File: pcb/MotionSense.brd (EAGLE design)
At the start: 59.4 x 59.2 mm, 14 parts

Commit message: [UPDATE] connection missing bug fixing
connection to the ground was not done.
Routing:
- net N$4: track 93.7 -> 106.0 mm
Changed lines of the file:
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@@
 <wire x1="70.7009" y1="65.4431" x2="61.9252" y2="65.4431" width="0.4064" layer="1"/>
 <wire x1="69.6976" y1="56.0451" x2="72.1741" y2="58.5216" width="0.4064" layer="1"/>
-<wire x1="69.394" y1="22.8748" x2="69.3432" y2="31.8156" width="0" layer="19" extent="1-1"/>
+<wire x1="69.394" y1="22.8748" x2="72.958959375" y2="26.439759375" width="0.4064" layer="16"/>
+<wire x1="72.958959375" y1="26.439759375" x2="72.958959375" y2="28.971240625" width="0.4064" layer="16"/>
+<wire x1="72.958959375" y1="28.971240625" x2="70.1146" y2="31.8156" width="0.4064" layer="16"/>
+<wire x1="70.1146" y1="31.8156" x2="69.3432" y2="31.8156" width="0.4064" layer="16"/>
 </signal>
 <signal name="N$5">

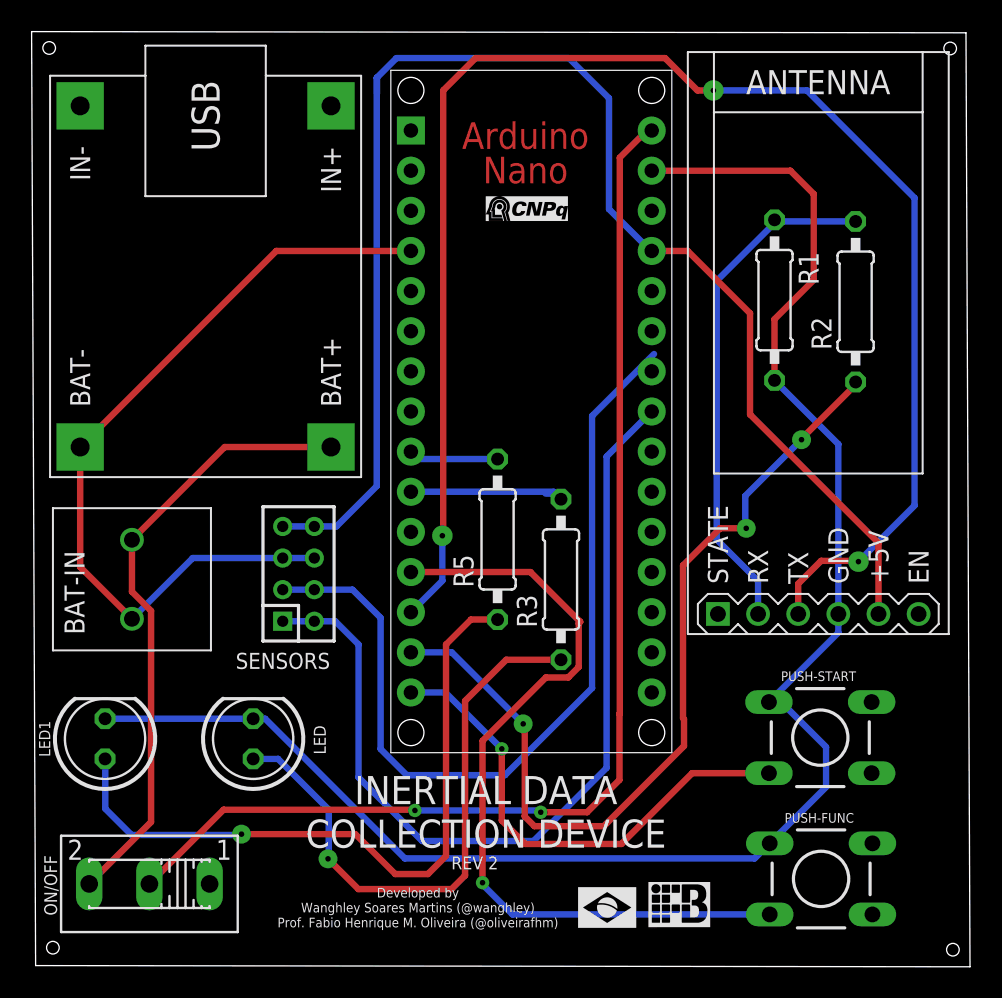
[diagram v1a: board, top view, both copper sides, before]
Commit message: [UPDATE]pads correction to up to 1.4mm
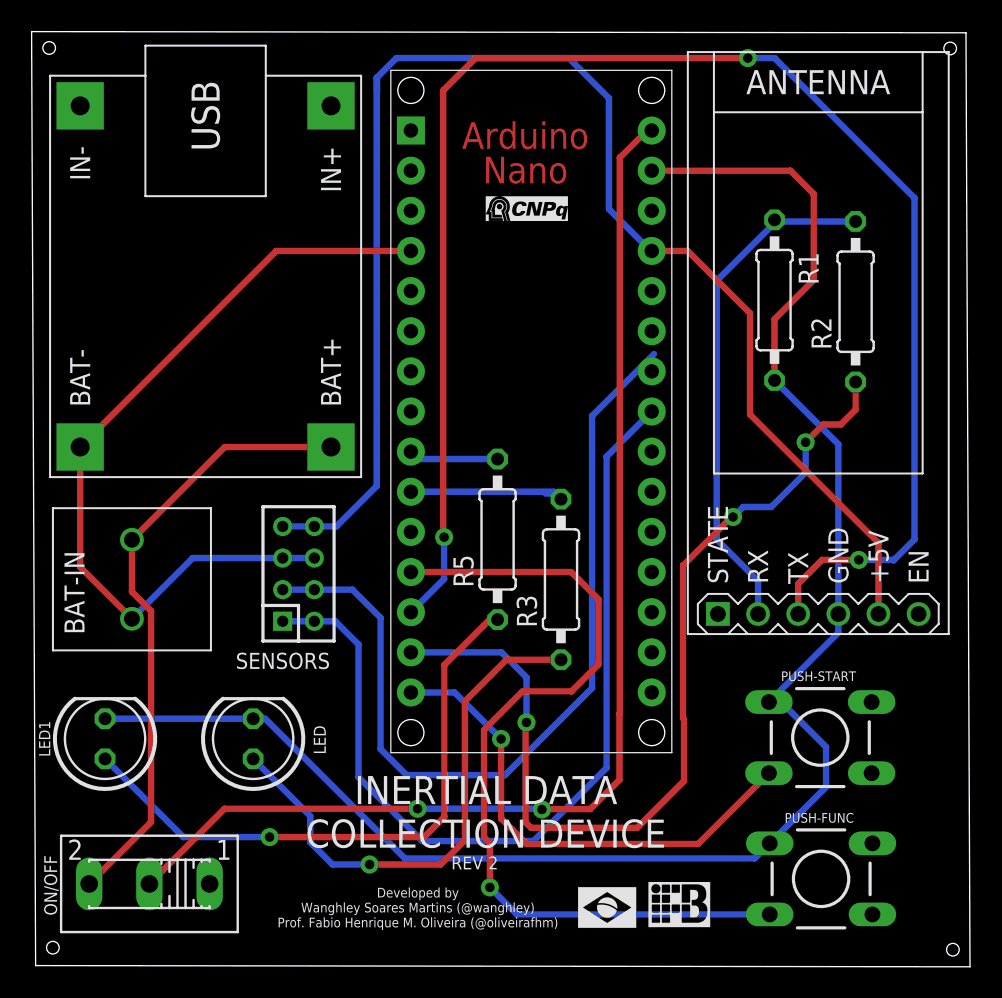
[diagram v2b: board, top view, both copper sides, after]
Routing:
- net N$14: track 44.3 -> 38.2 mm
- net N$3: track 56.1 -> 60.4 mm
- net N$1: track 37.3 -> 33.7 mm
- net N$12: track 51.0 -> 54.2 mm
- net N$5: track 99.2 -> 100.3 mm

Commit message: [UPDATE]projeting led RGB pcb connection and positionating
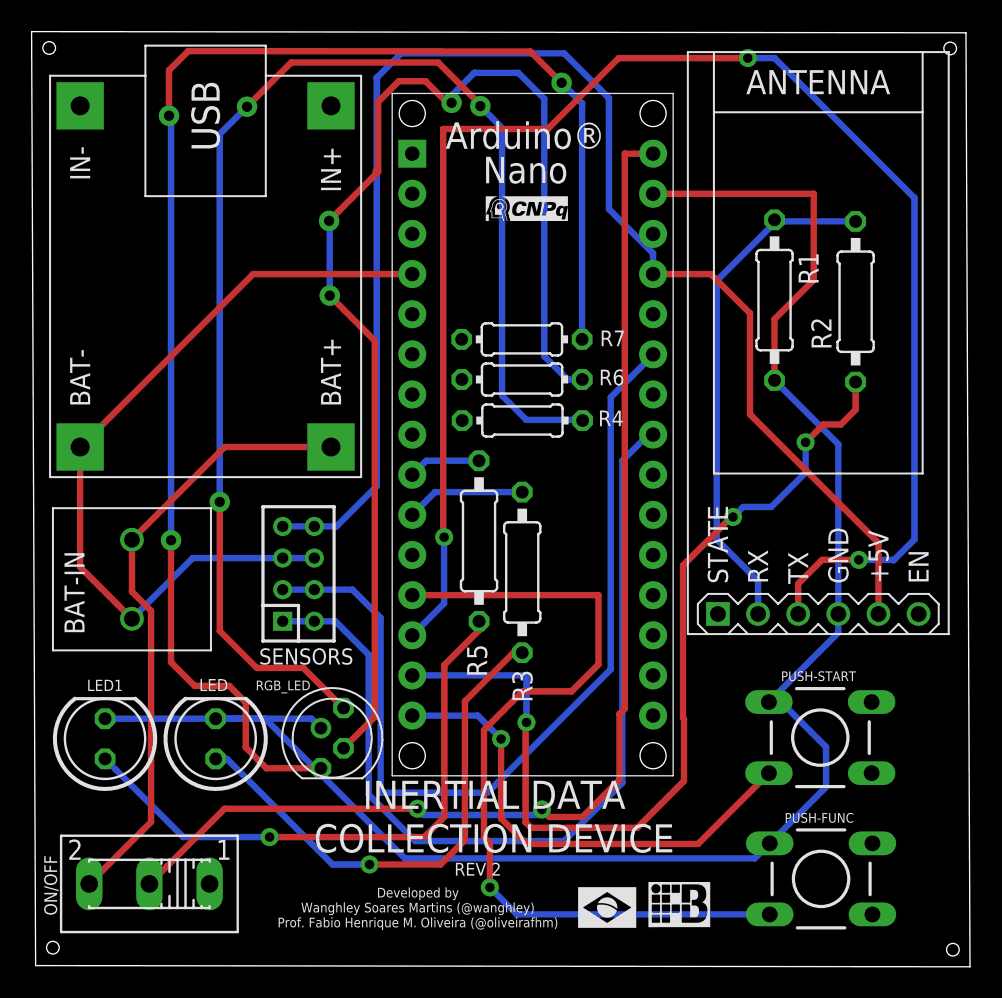
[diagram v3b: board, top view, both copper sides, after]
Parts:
- added R4, R6, R7: 120R, rcl:0204/7
- added RGB_LED: 5MMRGBLED, led_rgb:LED5MMRGB
- moved R3 2.49 mm to (53.7, 40.0)
- moved LED 2.37 mm to (34.3, 29.5)
- moved ARDUINO-NANO 1.47 mm to (54.4, 48.7)
- moved R5 1.18 mm to (51.0, 42.0)
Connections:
- new net N$17: R4.2, RGB_LED.P$4
- new net N$18: R6.2, RGB_LED.P$2
- new net N$19: R7.2, RGB_LED.P$1
- new net N$20: ARDUINO-NANO.J1.8, R4.1
- new net N$21: ARDUINO-NANO.J1.7, R6.1
- new net N$22: ARDUINO-NANO.J1.6, R7.1
- net N$4: now also RGB_LED.P$3
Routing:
- net N$19: track 0.00 -> 94.4 mm, vias 0 -> 3
- net N$17: track 0.00 -> 85.5 mm, vias 0 -> 3
- net N$18: track 0.00 -> 77.1 mm, vias 0 -> 3
- net N$4: track 106.0 -> 112.2 mm
- net N$9: track 10.8 -> 7.59 mm
- net N$7: track 54.4 -> 56.9 mm
- net N$13: track 5.68 -> 4.59 mm
- net N$2: track 91.2 -> 92.2 mm
- net N$14: track 38.2 -> 37.3 mm
- net N$1: track 33.7 -> 32.9 mm
- net N$10: track 31.4 -> 30.7 mm
- net N$3: track 60.4 -> 59.8 mm
- net N$12: track 54.2 -> 53.7 mm
- net NEGATIVE: track 51.4 -> 50.9 mm
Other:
- board text added: "Arduino® Nano"
- board text removed: "Arduino Nano"
